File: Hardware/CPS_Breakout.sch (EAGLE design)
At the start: 9 parts

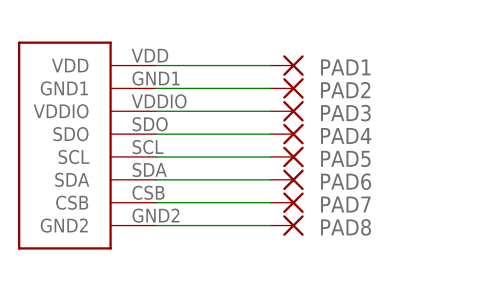
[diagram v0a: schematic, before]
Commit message: updated pinheaders and names
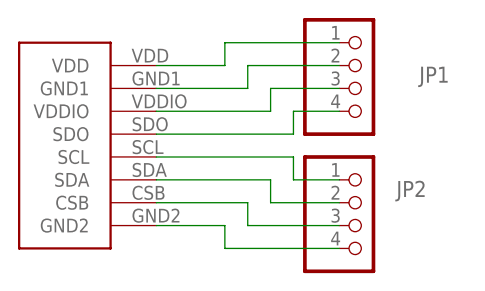
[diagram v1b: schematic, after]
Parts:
- removed PAD1, PAD2, PAD3, PAD4, PAD5, PAD6, PAD7, PAD8: (no value), wirepad:1,6/0,8
- added JP1, JP2: (no value), pinhead:PINHD-1X4
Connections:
- net N$1: now also B1.GND1, JP1.2; no longer B1.VDD, PAD1.P
- net N$2: now also B1.VDD, JP1.1; no longer B1.GND1, PAD2.P
- net N$3: now also JP1.3; no longer PAD3.P
- net N$4: now also JP1.4; no longer PAD4.P
- net N$5: now also JP2.1; no longer PAD5.P
- net N$6: now also JP2.2; no longer PAD6.P
- net N$7: now also JP2.3; no longer PAD7.P
- net N$8: now also JP2.4; no longer PAD8.P
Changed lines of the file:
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@@
 <parts>
 <part name="B1" library="CPS123" deviceset="CPS123" device=""/>
-<part name="PAD1" library="wirepad" library_urn="urn:adsk.eagle:library:412" deviceset="1,6/0,8" device="" package3d_urn="urn:adsk.eagle:package:30830/1"/>
-<part name="PAD2" library="wirepad" library_urn="urn:adsk.eagle:library:412" deviceset="1,6/0,8" device="" package3d_urn="urn:adsk.eagle:package:30830/1"/>
-<part name="PAD3" library="wirepad" library_urn="urn:adsk.eagle:library:412" deviceset="1,6/0,8" device="" package3d_urn="urn:adsk.eagle:package:30830/1"/>
-<part name="PAD4" library="wirepad" library_urn="urn:adsk.eagle:library:412" deviceset="1,6/0,8" device="" package3d_urn="urn:adsk.eagle:package:30830/1"/>
-<part name="PAD5" library="wirepad" library_urn="urn:adsk.eagle:library:412" deviceset="1,6/0,8" device="" package3d_urn="urn:adsk.eagle:package:30830/1"/>
-<part name="PAD6" library="wirepad" library_urn="urn:adsk.eagle:library:412" deviceset="1,6/0,8" device="" package3d_urn="urn:adsk.eagle:package:30830/1"/>
-<part name="PAD7" library="wirepad" library_urn="urn:adsk.eagle:library:412" deviceset="1,6/0,8" device="" package3d_urn="urn:adsk.eagle:package:30830/1"/>
-<part name="PAD8" library="wirepad" library_urn="urn:adsk.eagle:library:412" deviceset="1,6/0,8" device="" package3d_urn="urn:adsk.eagle:package:30830/1"/>
+<part name="JP1" library="pinhead" library_urn="urn:adsk.eagle:library:325" deviceset="PINHD-1X4" device="" package3d_urn="urn:adsk.eagle:package:22407/2"/>
+<part name="JP2" library="pinhead" library_urn="urn:adsk.eagle:library:325" deviceset="PINHD-1X4" device="" package3d_urn="urn:adsk.eagle:package:22407/2"/>
 </parts>
 <sheets>
@@
 <instances>
 <instance part="B1" gate="G$1" x="12.7" y="5.08" smashed="yes"/>
-<instance part="PAD1" gate="P" x="30.48" y="20.32" smashed="yes" rot="R180">
-<attribute name="NAME" x="39.243" y="21.0058" size="1.778" layer="95" rot="R180"/>
-<attribute name="VALUE" x="31.623" y="23.622" size="1.778" layer="96" rot="R180"/>
+<instance part="JP1" gate="A" x="38.1" y="17.78" smashed="yes">
+<attribute name="NAME" x="44.45" y="18.415" size="1.778" layer="95"/>
+<attribute name="VALUE" x="31.75" y="10.16" size="1.778" layer="96"/>
 </instance>
-<instance part="PAD2" gate="P" x="30.48" y="17.78" smashed="yes" rot="R180">
-<attribute name="NAME" x="39.243" y="18.4658" size="1.778" layer="95" rot="R180"/>
-<attribute name="VALUE" x="31.623" y="21.082" size="1.778" layer="96" rot="R180"/>
-</instance>
-<instance part="PAD3" gate="P" x="30.48" y="15.24" smashed="yes" rot="R180">
-<attribute name="NAME" x="39.243" y="15.9258" size="1.778" layer="95" rot="R180"/>
-<attribute name="VALUE" x="31.623" y="18.542" size="1.778" layer="96" rot="R180"/>
-</instance>
-<instance part="PAD4" gate="P" x="30.48" y="12.7" smashed="yes" rot="R180">
-<attribute name="NAME" x="39.243" y="13.3858" size="1.778" layer="95" rot="R180"/>
-<attribute name="VALUE" x="31.623" y="16.002" size="1.778" layer="96" rot="R180"/>
-</instance>
-<instance part="PAD5" gate="P" x="30.48" y="10.16" smashed="yes" rot="R180">
-<attribute name="NAME" x="39.243" y="10.8458" size="1.778" layer="95" rot="R180"/>
-<attribute name="VALUE" x="31.623" y="13.462" size="1.778" layer="96" rot="R180"/>
-</instance>
-<instance part="PAD6" gate="P" x="30.48" y="7.62" smashed="yes" rot="R180">
-<attribute name="NAME" x="39.243" y="8.3058" size="1.778" layer="95" rot="R180"/>
-<attribute name="VALUE" x="31.623" y="10.922" size="1.778" layer="96" rot="R180"/>
-</instance>
-<instance part="PAD7" gate="P" x="30.48" y="5.08" smashed="yes" rot="R180">
-<attribute name="NAME" x="39.243" y="5.7658" size="1.778" layer="95" rot="R180"/>
-<attribute name="VALUE" x="31.623" y="8.382" size="1.778" layer="96" rot="R180"/>
-</instance>
-<instance part="PAD8" gate="P" x="30.48" y="2.54" smashed="yes" rot="R180">
-<attribute name="NAME" x="39.243" y="3.2258" size="1.778" layer="95" rot="R180"/>
-<attribute name="VALUE" x="31.623" y="5.842" size="1.778" layer="96" rot="R180"/>
+<instance part="JP2" gate="A" x="38.1" y="2.54" smashed="yes">
+<attribute name="NAME" x="41.91" y="5.715" size="1.778" layer="95"/>
+<attribute name="VALUE" x="31.75" y="-5.08" size="1.778" layer="96"/>
 </instance>
 </instances>
@@
 </busses>
 <nets>
-<net name="N$1" class="0">
-<segment>
-<pinref part="B1" gate="G$1" pin="VDD"/>
-<pinref part="PAD1" gate="P" pin="P"/>
-<wire x1="15.24" y1="20.32" x2="27.94" y2="20.32" width="0.1524" layer="91"/>
-</segment>
-</net>
-<net name="N$2" class="0">
-<segment>
-<pinref part="B1" gate="G$1" pin="GND1"/>
-<pinref part="PAD2" gate="P" pin="P"/>
-<wire x1="15.24" y1="17.78" x2="27.94" y2="17.78" width="0.1524" layer="91"/>
-</segment>
-</net>
 <net name="N$3" class="0">
 <segment>
 <pinref part="B1" gate="G$1" pin="VDDIO"/>
-<pinref part="PAD3" gate="P" pin="P"/>
 <wire x1="15.24" y1="15.24" x2="27.94" y2="15.24" width="0.1524" layer="91"/>
+<wire x1="27.94" y1="15.24" x2="27.94" y2="17.78" width="0.1524" layer="91"/>
+<pinref part="JP1" gate="A" pin="3"/>
+<wire x1="27.94" y1="17.78" x2="35.56" y2="17.78" width="0.1524" layer="91"/>
 </segment>
 </net>
@@
 <segment>
 <pinref part="B1" gate="G$1" pin="SDO"/>
-<pinref part="PAD4" gate="P" pin="P"/>
-<wire x1="15.24" y1="12.7" x2="27.94" y2="12.7" width="0.1524" layer="91"/>
+<wire x1="15.24" y1="12.7" x2="30.48" y2="12.7" width="0.1524" layer="91"/>
+<wire x1="30.48" y1="12.7" x2="30.48" y2="15.24" width="0.1524" layer="91"/>
+<pinref part="JP1" gate="A" pin="4"/>
+<wire x1="30.48" y1="15.24" x2="35.56" y2="15.24" width="0.1524" layer="91"/>
 </segment>
 </net>
@@
 <segment>
 <pinref part="B1" gate="G$1" pin="SCL"/>
-<pinref part="PAD5" gate="P" pin="P"/>
-<wire x1="15.24" y1="10.16" x2="27.94" y2="10.16" width="0.1524" layer="91"/>
+<wire x1="15.24" y1="10.16" x2="30.48" y2="10.16" width="0.1524" layer="91"/>
+<wire x1="30.48" y1="10.16" x2="30.48" y2="7.62" width="0.1524" layer="91"/>
+<pinref part="JP2" gate="A" pin="1"/>
+<wire x1="30.48" y1="7.62" x2="35.56" y2="7.62" width="0.1524" layer="91"/>
 </segment>
 </net>
@@
 <segment>
 <pinref part="B1" gate="G$1" pin="SDA"/>
-<pinref part="PAD6" gate="P" pin="P"/>
 <wire x1="15.24" y1="7.62" x2="27.94" y2="7.62" width="0.1524" layer="91"/>
+<wire x1="27.94" y1="7.62" x2="27.94" y2="5.08" width="0.1524" layer="91"/>
+<pinref part="JP2" gate="A" pin="2"/>
+<wire x1="27.94" y1="5.08" x2="35.56" y2="5.08" width="0.1524" layer="91"/>
+</segment>
+</net>
+<net name="N$1" class="0">
+<segment>
+<pinref part="B1" gate="G$1" pin="GND1"/>
+<wire x1="15.24" y1="17.78" x2="25.4" y2="17.78" width="0.1524" layer="91"/>
+<wire x1="25.4" y1="17.78" x2="25.4" y2="20.32" width="0.1524" layer="91"/>
+<pinref part="JP1" gate="A" pin="2"/>
+<wire x1="25.4" y1="20.32" x2="35.56" y2="20.32" width="0.1524" layer="91"/>
+</segment>
+</net>
+<net name="N$2" class="0">
+<segment>
+<pinref part="B1" gate="G$1" pin="VDD"/>
+<wire x1="15.24" y1="20.32" x2="22.86" y2="20.32" width="0.1524" layer="91"/>
+<wire x1="22.86" y1="20.32" x2="22.86" y2="22.86" width="0.1524" layer="91"/>
+<pinref part="JP1" gate="A" pin="1"/>
+<wire x1="22.86" y1="22.86" x2="35.56" y2="22.86" width="0.1524" layer="91"/>
 </segment>
 </net>
@@
 <segment>
 <pinref part="B1" gate="G$1" pin="CSB"/>
-<pinref part="PAD7" gate="P" pin="P"/>
-<wire x1="15.24" y1="5.08" x2="27.94" y2="5.08" width="0.1524" layer="91"/>
+<wire x1="15.24" y1="5.08" x2="25.4" y2="5.08" width="0.1524" layer="91"/>
+<wire x1="25.4" y1="5.08" x2="25.4" y2="2.54" width="0.1524" layer="91"/>
+<pinref part="JP2" gate="A" pin="3"/>
+<wire x1="25.4" y1="2.54" x2="35.56" y2="2.54" width="0.1524" layer="91"/>
 </segment>
 </net>
@@
 <segment>
 <pinref part="B1" gate="G$1" pin="GND2"/>
-<pinref part="PAD8" gate="P" pin="P"/>
-<wire x1="15.24" y1="2.54" x2="27.94" y2="2.54" width="0.1524" layer="91"/>
+<wire x1="15.24" y1="2.54" x2="22.86" y2="2.54" width="0.1524" layer="91"/>
+<wire x1="22.86" y1="2.54" x2="22.86" y2="0" width="0.1524" layer="91"/>
+<pinref part="JP2" gate="A" pin="4"/>
+<wire x1="22.86" y1="0" x2="35.56" y2="0" width="0.1524" layer="91"/>
 </segment>
 </net>
